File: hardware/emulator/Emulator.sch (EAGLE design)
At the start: 29 parts, among them T2 2N5401, U1 PDM1-S5-D12-S, U2 LM6132BIN, U3 OPA2277PA, U4 L7908CV, U5 L7808ABV, U6 TEENSY_3.6_DIL, U7 ZVP2106ASTZ

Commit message: Migrate emulator board to Teensy 4.1
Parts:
- removed D1, D2: 3v3, diode:ZENER-DIODEZD-7.5
- removed LED_PWR: (no value), led:LED5MM
- removed U1: PDM1-S5-D12-S, PDM1-S5-D12-S:PDM1-S5-D12-S
- removed U6: TEENSY_3.6_DIL, Teensy_3_and_LC_Series_Boards_v1.4:TEENSY_3.6_DIL
- added C10, C12, C8: 0.1u, rcl:C-EU025-024X044
- added C11: 0.33u, rcl:C-EU025-024X044
- added C13: 2.2u, rcl:C-EU025-024X044
- added C14: 1u, rcl:C-EU025-024X044
- added C15: 200p, rcl:C-EU025-024X044
- added C9: 10u, rcl:C-EU025-024X044
- added MODE: (no value), con-lstb:MA03-1
- added POWER, STATUS: (no value), led:LED5MM
- added PS1: RD-0512D, RD-0512D:RD-0512D
- added R6: 330R, rcl:R-EU_0207/10
- added U8: DEV-16771_REDUCED_PINS, DEV-16771 (Teensy 41):DEV-16771_REDUCED_PINS
- added U9: MCP4822-E/P, MCP4822-E_P:MCP4822-E/P
- C1, C5, C6: device rcl:CPOL-EUE2-4 -> rcl:C-EU025-024X044
- C2, C3: device rcl:CPOL-EUE2-5 -> rcl:C-EU025-024X044
- C4: value 1u -> 0.1u; device rcl:CPOL-EUE2-5 -> rcl:C-EU025-024X044
- C7: value 10pF -> 10p; device rcl:C-EU050-025X075 -> rcl:C-EU025-024X044
- R_RANGE: value 51 -> 51R
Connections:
- removed net N$4: D1.C, D2.A
- removed net N$8: R4.1, R5.2, U3.INA-
- new net +5V: C1.1, C8.1, C9.1, PS1.+VIN, U8.VIN, U9.VDD
- new net DAC_CS: U8.RX8, U9.!CS
- new net DAC_MOSI: U8.MOSI, U9.SDI
- new net DAC_SCK: U8.SCK, U9.SCK
- new net JUMPER_SELECT_MODE: MODE.2, U8.OUT1B
- new net N$3: C15.1, R4.1, R5.2, U3.INA-
- new net STATUS_LED: R6.2, U8.TX1
- net +12V: now also C11.1, C2.1, PS1.+VOUT; no longer C2.+, U1.+VO
- net +3V3: now also MODE.3, U8.3.3V; no longer U6.3.3V
- net +8V: now also C10.2, C12.2, C5.2; no longer C5.+
- net -12V: now also C13.2, C3.1, PS1.-VOUT; no longer C3.-, U1.-VO
- net -8V: now also C14.2, C4.2; no longer C4.-
- net DAC_OC_VOLTAGE_EMULATION: now also U9.VOUTA; no longer U6.A22/DAC1
- net DAC_SC_CURRENT_EMULATION: now also U9.VOUTB; no longer U6.A21/DAC0
- net GND: now also C1.2, C10.1, C11.2, C12.1, C13.1, C14.1, C2.2, C3.2, C4.1, C5.1, C6.1, C8.2, C9.2, MODE.1, POWER.C, PS1.-VIN, PS1.COM, STATUS.C, U8.GND, U9.!LDAC, U9.AVSS; no longer C1.-, C2.-, C3.+, C4.+, C5.-, C6.-, D1.A, LED_PWR.C, U1.0V, U1.GND, U6.GND
- net HARVESTER_EMULATION: now also C6.2; no longer C6.+, D2.C
- net N$2: now also R6.1, STATUS.A; no longer C1.+, U1.VIN, U6.VIN
- net N$6: now also C15.2
- net N$9: now also POWER.A; no longer LED_PWR.A
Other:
- note added: "Maximum Emulation Current: 3.3 / R_Range Example: 3.3 / 51 = 0.064705 A = 64.7 mA"
- note removed: "Maximum Emulation Current: 3.3 / R_Range Example: 3.3 / 51 = 0,064705 A = 64,7 mA"

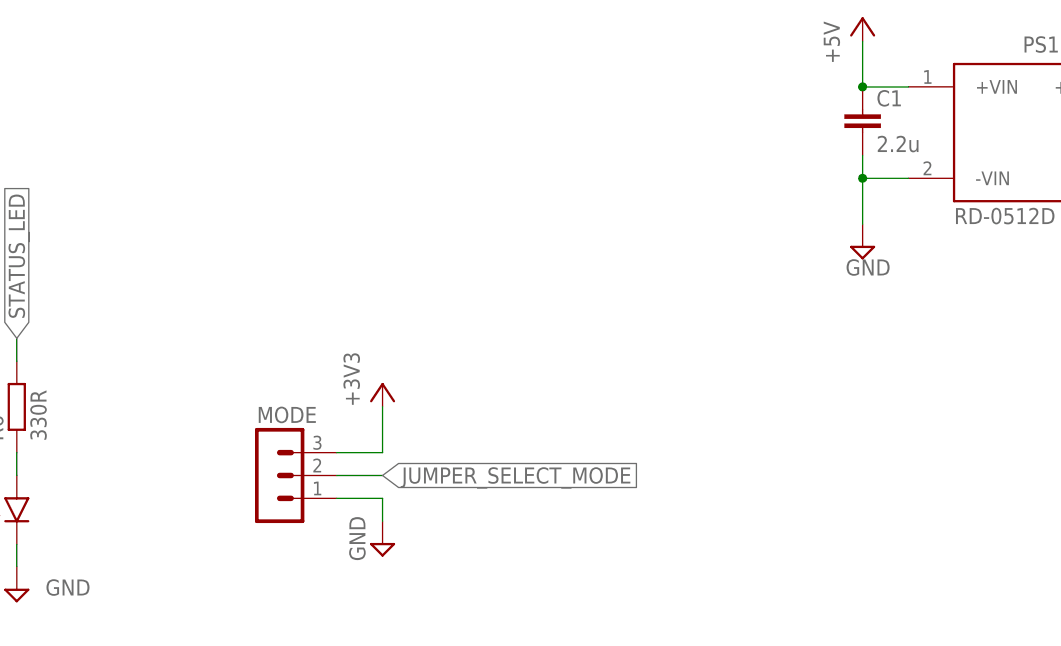
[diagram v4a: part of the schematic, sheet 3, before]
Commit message: Add error LED to the board
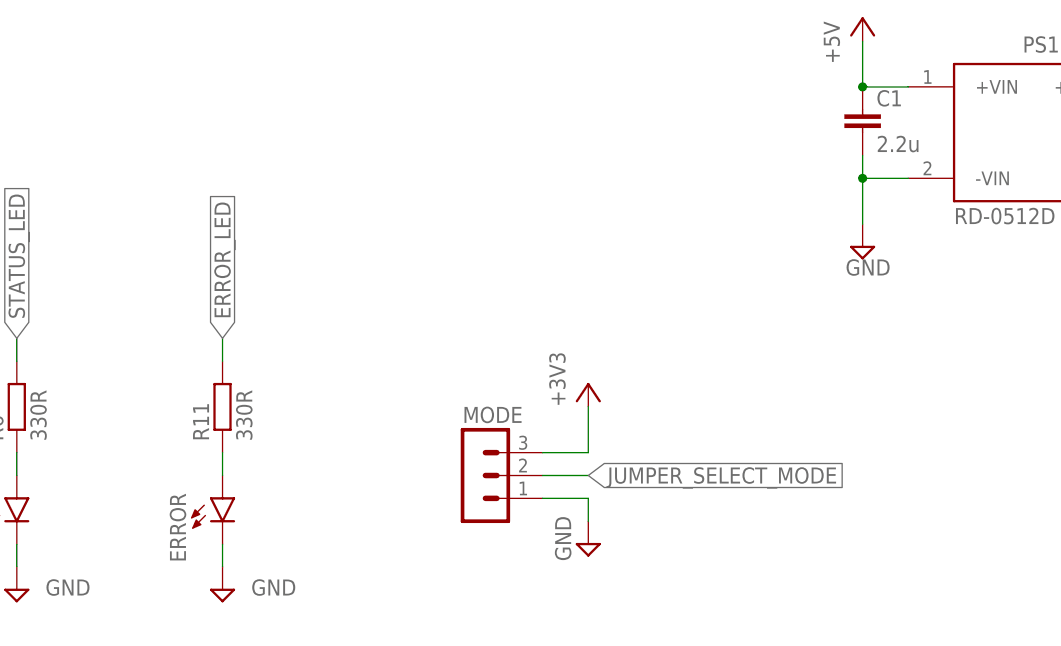
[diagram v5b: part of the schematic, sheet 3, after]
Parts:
- added ERROR: (no value), led:LED5MM
- added R11: 330R, rcl:R-EU_0207/10
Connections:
- new net ERROR_LED: R11.2, U8.OUT2
- new net N$4: ERROR.A, R11.1
- net GND: now also ERROR.C
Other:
- moved on the sheet: MODE
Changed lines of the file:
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@@
 <part name="C14" library="rcl" library_urn="urn:adsk.eagle:library:334" deviceset="C-EU" device="025-024X044" package3d_urn="urn:adsk.eagle:package:23630/1" value="1u"/>
 <part name="C15" library="rcl" library_urn="urn:adsk.eagle:library:334" deviceset="C-EU" device="025-024X044" package3d_urn="urn:adsk.eagle:package:23630/1" value="200p"/>
+<part name="SUPPLY30" library="supply2" library_urn="urn:adsk.eagle:library:372" deviceset="GND" device=""/>
+<part name="R11" library="rcl" library_urn="urn:adsk.eagle:library:334" deviceset="R-EU_" device="0207/10" package3d_urn="urn:adsk.eagle:package:23491/2" value="330R"/>
+<part name="ERROR" library="led" library_urn="urn:adsk.eagle:library:259" deviceset="LED" device="5MM" package3d_urn="urn:adsk.eagle:package:15799/2"/>
 </parts>
 <sheets>
@@
 <wire x1="137.16" y1="104.14" x2="139.7" y2="104.14" width="0.1524" layer="91"/>
 <label x="139.7" y="104.14" size="1.778" layer="95" xref="yes"/>
+</segment>
+</net>
+<net name="ERROR_LED" class="0">
+<segment>
+<pinref part="U8" gate="G$1" pin="OUT2"/>
+<wire x1="137.16" y1="111.76" x2="139.7" y2="111.76" width="0.1524" layer="91"/>
+<label x="139.7" y="111.76" size="1.778" layer="95" xref="yes"/>
 </segment>
 </net>
@@
 <attribute name="VALUE" x="81.915" y="28.448" size="1.778" layer="96" rot="R90"/>
 </instance>
-<instance part="MODE" gate="G$1" x="104.14" y="35.56" smashed="yes">
-<attribute name="VALUE" x="102.87" y="27.94" size="1.778" layer="96"/>
-<attribute name="NAME" x="102.87" y="41.402" size="1.778" layer="95"/>
-</instance>
-<instance part="+3V4" gate="G$1" x="116.84" y="45.72" smashed="yes">
-<attribute name="VALUE" x="114.3" y="43.18" size="1.778" layer="96" rot="R90"/>
-</instance>
-<instance part="SUPPLY9" gate="GND" x="116.84" y="27.94" smashed="yes">
-<attribute name="VALUE" x="114.935" y="26.035" size="1.778" layer="96" rot="R90"/>
+<instance part="MODE" gate="G$1" x="127" y="35.56" smashed="yes">
+<attribute name="VALUE" x="125.73" y="27.94" size="1.778" layer="96"/>
+<attribute name="NAME" x="125.73" y="41.402" size="1.778" layer="95"/>
+</instance>
+<instance part="+3V4" gate="G$1" x="139.7" y="45.72" smashed="yes">
+<attribute name="VALUE" x="137.16" y="43.18" size="1.778" layer="96" rot="R90"/>
+</instance>
+<instance part="SUPPLY9" gate="GND" x="139.7" y="27.94" smashed="yes">
+<attribute name="VALUE" x="137.795" y="26.035" size="1.778" layer="96" rot="R90"/>
 </instance>
 <instance part="C11" gate="G$1" x="152.4" y="142.24" smashed="yes">
@@
 <attribute name="NAME" x="152.781" y="112.776" size="1.778" layer="95" rot="R270"/>
 <attribute name="VALUE" x="160.401" y="112.776" size="1.778" layer="96" rot="R270"/>
+</instance>
+<instance part="SUPPLY30" gate="GND" x="99.06" y="22.86" smashed="yes">
+<attribute name="VALUE" x="102.235" y="22.225" size="1.778" layer="96"/>
+</instance>
+<instance part="R11" gate="G$1" x="99.06" y="43.18" smashed="yes" rot="R90">
+<attribute name="NAME" x="97.5614" y="39.37" size="1.778" layer="95" rot="R90"/>
+<attribute name="VALUE" x="102.362" y="39.37" size="1.778" layer="96" rot="R90"/>
+</instance>
+<instance part="ERROR" gate="G$1" x="99.06" y="33.02" smashed="yes">
+<attribute name="NAME" x="94.996" y="25.908" size="1.778" layer="95" rot="R90"/>
+<attribute name="VALUE" x="104.775" y="28.448" size="1.778" layer="96" rot="R90"/>
 </instance>
 </instances>
@@
 <pinref part="MODE" gate="G$1" pin="1"/>
 <pinref part="SUPPLY9" gate="GND" pin="GND"/>
-<wire x1="111.76" y1="33.02" x2="116.84" y2="33.02" width="0.1524" layer="91"/>
-<wire x1="116.84" y1="33.02" x2="116.84" y2="30.48" width="0.1524" layer="91"/>
+<wire x1="134.62" y1="33.02" x2="139.7" y2="33.02" width="0.1524" layer="91"/>
+<wire x1="139.7" y1="33.02" x2="139.7" y2="30.48" width="0.1524" layer="91"/>
 </segment>
 <segment>
@@
 <pinref part="SUPPLY29" gate="GND" pin="GND"/>
 <wire x1="157.48" y1="106.68" x2="157.48" y2="104.14" width="0.1524" layer="91"/>
+</segment>
+<segment>
+<pinref part="SUPPLY30" gate="GND" pin="GND"/>
+<pinref part="ERROR" gate="G$1" pin="C"/>
+<wire x1="99.06" y1="25.4" x2="99.06" y2="27.94" width="0.1524" layer="91"/>
 </segment>
 </net>
@@
 <pinref part="MODE" gate="G$1" pin="3"/>
 <pinref part="+3V4" gate="G$1" pin="+3V3"/>
-<wire x1="111.76" y1="38.1" x2="116.84" y2="38.1" width="0.1524" layer="91"/>
-<wire x1="116.84" y1="38.1" x2="116.84" y2="43.18" width="0.1524" layer="91"/>
+<wire x1="134.62" y1="38.1" x2="139.7" y2="38.1" width="0.1524" layer="91"/>
+<wire x1="139.7" y1="38.1" x2="139.7" y2="43.18" width="0.1524" layer="91"/>
 </segment>
 </net>
@@
 <segment>
 <pinref part="MODE" gate="G$1" pin="2"/>
-<wire x1="111.76" y1="35.56" x2="116.84" y2="35.56" width="0.1524" layer="91"/>
-<label x="116.84" y="35.56" size="1.778" layer="95" xref="yes"/>
-</segment>
-</net>
+<wire x1="134.62" y1="35.56" x2="139.7" y2="35.56" width="0.1524" layer="91"/>
+<label x="139.7" y="35.56" size="1.778" layer="95" xref="yes"/>
+</segment>
+</net>
+<net name="N$4" class="0">
+<segment>
+<pinref part="R11" gate="G$1" pin="1"/>
+<pinref part="ERROR" gate="G$1" pin="A"/>
+<wire x1="99.06" y1="38.1" x2="99.06" y2="35.56" width="0.1524" layer="91"/>
+</segment>
+</net>
+<net name="ERROR_LED" class="0">
+<segment>
+<pinref part="R11" gate="G$1" pin="2"/>
+<wire x1="99.06" y1="48.26" x2="99.06" y2="50.8" width="0.1524" layer="91"/>
+<label x="99.06" y="50.8" size="1.778" layer="95" rot="R90" xref="yes"/>
+</segment>
+</net>

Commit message: Add minor changes to the hardware
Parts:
- R_RANGE: value 51R -> 49R9
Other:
- note added: "Maximum Emulation Current: 3.3 / R_Range Example: 3.3 / 49.9 = 0.0661322 A = 66.13 mA"
- note removed: "Maximum Emulation Current: 3.3 / R_Range Example: 3.3 / 51 = 0.064705 A = 64.7 mA"
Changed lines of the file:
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@@
 <part name="R4" library="rcl" library_urn="urn:adsk.eagle:library:334" deviceset="R-EU_" device="0207/10" package3d_urn="urn:adsk.eagle:package:23491/2" value="10k"/>
 <part name="R5" library="rcl" library_urn="urn:adsk.eagle:library:334" deviceset="R-EU_" device="0207/10" package3d_urn="urn:adsk.eagle:package:23491/2" value="10k"/>
-<part name="R_RANGE" library="rcl" library_urn="urn:adsk.eagle:library:334" deviceset="R-EU_" device="0207/10" package3d_urn="urn:adsk.eagle:package:23491/2" value="51R"/>
+<part name="R_RANGE" library="rcl" library_urn="urn:adsk.eagle:library:334" deviceset="R-EU_" device="0207/10" package3d_urn="urn:adsk.eagle:package:23491/2" value="49R9"/>
 <part name="R7" library="rcl" library_urn="urn:adsk.eagle:library:334" deviceset="R-EU_" device="0207/10" package3d_urn="urn:adsk.eagle:package:23491/2" value="100R"/>
 <part name="SUPPLY8" library="supply2" library_urn="urn:adsk.eagle:library:372" deviceset="GND" device=""/>
@@
 <text x="109.22" y="134.62" size="1.778" layer="97">Solar Cell Model</text>
 <text x="73.66" y="157.48" size="1.778" layer="97">Maximum Emulation Current: 3.3 / R_Range
-Example: 3.3 / 51 = 0.064705 A = 64.7 mA</text>
+Example: 3.3 / 49.9 = 0.0661322 A = 66.13 mA</text>
 <text x="50.8" y="121.92" size="1.778" layer="97">I_OUT = DAC_SC / R_RANGE</text>
 </plain>
@@
 <instance part="R_RANGE" gate="G$1" x="50.8" y="160.02" smashed="yes" rot="R180">
 <attribute name="NAME" x="54.61" y="158.5214" size="1.778" layer="95" rot="R180"/>
-<attribute name="VALUE" x="52.07" y="163.322" size="1.778" layer="96" rot="R180"/>
+<attribute name="VALUE" x="54.61" y="163.322" size="1.778" layer="96" rot="R180"/>
 </instance>
 <instance part="R7" gate="G$1" x="45.72" y="121.92" smashed="yes" rot="R270">

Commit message: Update part designators
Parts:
- removed U9: MCP4822-E/P, MCP4822-E_P:MCP4822-E/P
- added U6: L7908CV, L7908CV:L7908CV
- C1: value 2.2u -> 200p
- C10: value 0.1u -> 2.2u
- C12: value 0.1u -> 1u
- C15: value 200p -> 1u
- C2: value 1u -> 0.1u
- C3: value 1u -> 10p
- C5: value 0.1u -> 10u
- C7: value 10p -> 0.1u
- C9: value 10u -> 0.1u
- R10: value 100R -> 330R
- R3: value 330R -> 10k
- R5: value 10k -> 100R
- R6: value 330R -> 240k
- R7: value 100R -> 120k
- R8: value 120k -> 100R
- R9: value 240k -> 330R
- U2: value LM6132BIN -> OPA2277PA; device LM6132BIN:LM6132BIN -> OPA2277PA:OPA2277PA
- U3: value OPA2277PA -> MCP4822-E/P; device OPA2277PA:OPA2277PA -> MCP4822-E_P:MCP4822-E/P
- U4: value L7908CV -> LM6132BIN; device L7908CV:L7908CV -> LM6132BIN:LM6132BIN
- renumbered U7 to T1, U8 to U1
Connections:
- net +12V: now also C14.1; no longer C2.1
- net +3V3: now also R9.2; no longer R3.2
- net +5V: now also C13.1, C5.1, C6.1, U3.VDD; no longer C1.1, C8.1, C9.1, U9.VDD
- net +8V: now also C4.2, C7.2, C9.2, U2.V+, U4.+V; no longer C10.2, C12.2, C5.2, U2.+V, U3.V+
- net -12V: now also C10.2, C15.1, U6.IN; no longer C13.2, C3.1, U4.IN
- net -8V: now also C12.2, C2.2, U2.V-, U6.OUT; no longer C14.2, C4.2, U3.V-, U4.OUT
- net DAC_CS: now also U3.!CS; no longer U9.!CS
- net DAC_MOSI: now also U3.SDI; no longer U9.SDI
- net DAC_OC_VOLTAGE_EMULATION: now also U3.VOUTA, U4.+INB; no longer U2.+INB, U9.VOUTA
- net DAC_OC_VOLTAGE_EMULATION_BUFFERED: now also U2.INB+, U4.-INB, U4.OUT_B; no longer U2.-INB, U2.OUT_B, U3.INB+
- net DAC_SCK: now also U3.SCK; no longer U9.SCK
- net DAC_SC_CURRENT_EMULATION: now also U3.VOUTB, U4.+INA; no longer U2.+INA, U9.VOUTB
- net DAC_SC_CURRENT_EMULATION_BUFFERED: now also R3.2, U4.-INA, U4.OUT_A; no longer R4.2, U2.-INA, U2.OUT_A
- net GND: now also C13.2, C14.2, C15.2, C2.1, C5.2, C6.2, C7.1, C8.1, C9.1, R7.1, U3.!LDAC, U3.AVSS, U4.-V, U6.GND; no longer C1.2, C13.1, C14.1, C2.2, C3.2, C5.1, C6.1, C8.2, C9.2, R8.1, U2.-V, U4.GND, U9.!LDAC, U9.AVSS
- net HARVESTER_EMULATION: now also C8.2, R6.2; no longer C6.2, R9.2
- net N$1: now also U2.INA+; no longer U3.INA+
- net N$11: now also C3.1, R6.1, R7.2, U2.INB-; no longer C7.1, R8.2, R9.1, U3.INB-
- net N$12: now also R8.2; no longer R10.2
- net N$13: now also C3.2, R8.1, U2.OUTB; no longer C7.2, R10.1, U3.OUTB
- net N$2: now also R10.1; no longer R6.1
- net N$3: now also C1.1, R3.1, R4.2, U2.INA-; no longer C15.1, R4.1, R5.2, U3.INA-
- net N$5: now also R5.1; no longer R7.1
- net N$6: now also C1.2, R5.2, U2.OUTA; no longer C15.2, R7.2, U3.OUTA
- net N$7: now also R4.1; no longer R5.1
- net N$9: now also R9.1; no longer R3.1
- net STATUS_LED: now also R10.2; no longer R6.2

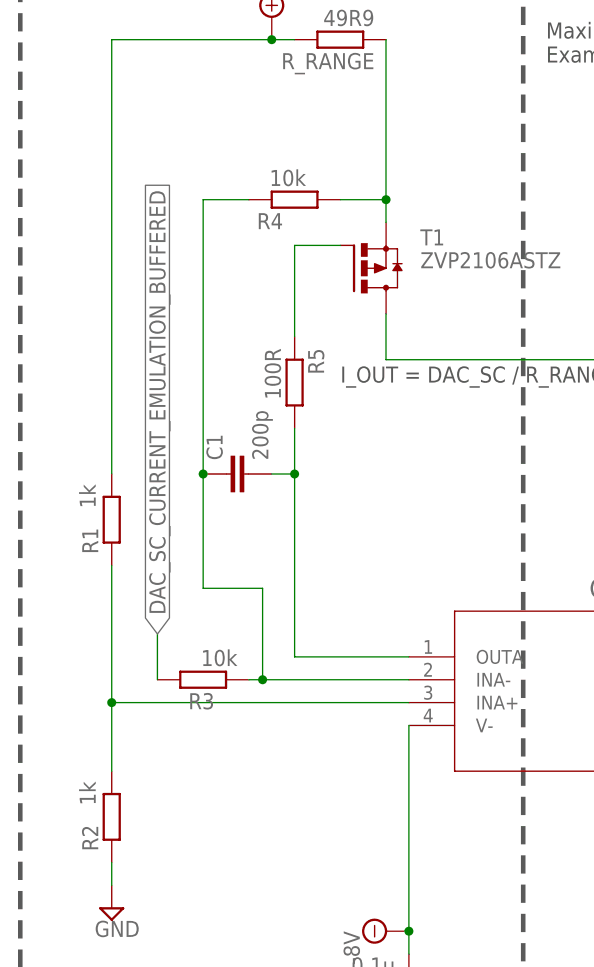
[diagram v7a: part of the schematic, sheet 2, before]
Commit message: Update resistor values
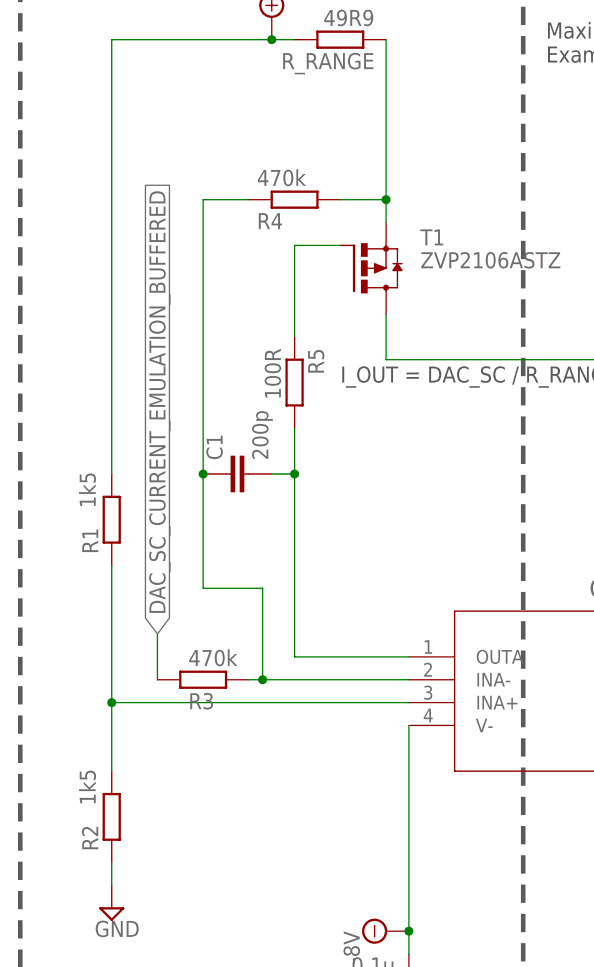
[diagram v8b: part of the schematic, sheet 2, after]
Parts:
- R1, R2: value 1k -> 1k5
- R3, R4: value 10k -> 470k
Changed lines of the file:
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@@
 <part name="SUPPLY17" library="supply2" library_urn="urn:adsk.eagle:library:372" deviceset="-8V" device=""/>
 <part name="U2" library="OPA2277PA" deviceset="OPA2277PA" device=""/>
-<part name="R1" library="rcl" library_urn="urn:adsk.eagle:library:334" deviceset="R-EU_" device="0207/10" package3d_urn="urn:adsk.eagle:package:23491/2" value="1k"/>
-<part name="R2" library="rcl" library_urn="urn:adsk.eagle:library:334" deviceset="R-EU_" device="0207/10" package3d_urn="urn:adsk.eagle:package:23491/2" value="1k"/>
-<part name="R3" library="rcl" library_urn="urn:adsk.eagle:library:334" deviceset="R-EU_" device="0207/10" package3d_urn="urn:adsk.eagle:package:23491/2" value="10k"/>
-<part name="R4" library="rcl" library_urn="urn:adsk.eagle:library:334" deviceset="R-EU_" device="0207/10" package3d_urn="urn:adsk.eagle:package:23491/2" value="10k"/>
+<part name="R1" library="rcl" library_urn="urn:adsk.eagle:library:334" deviceset="R-EU_" device="0207/10" package3d_urn="urn:adsk.eagle:package:23491/2" value="1k5"/>
+<part name="R2" library="rcl" library_urn="urn:adsk.eagle:library:334" deviceset="R-EU_" device="0207/10" package3d_urn="urn:adsk.eagle:package:23491/2" value="1k5"/>
+<part name="R3" library="rcl" library_urn="urn:adsk.eagle:library:334" deviceset="R-EU_" device="0207/10" package3d_urn="urn:adsk.eagle:package:23491/2" value="470k"/>
+<part name="R4" library="rcl" library_urn="urn:adsk.eagle:library:334" deviceset="R-EU_" device="0207/10" package3d_urn="urn:adsk.eagle:package:23491/2" value="470k"/>
 <part name="R_RANGE" library="rcl" library_urn="urn:adsk.eagle:library:334" deviceset="R-EU_" device="0207/10" package3d_urn="urn:adsk.eagle:package:23491/2" value="49R9"/>
 <part name="R5" library="rcl" library_urn="urn:adsk.eagle:library:334" deviceset="R-EU_" device="0207/10" package3d_urn="urn:adsk.eagle:package:23491/2" value="100R"/>
